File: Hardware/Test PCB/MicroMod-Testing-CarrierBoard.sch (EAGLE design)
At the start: 61 parts, among them J11 microSD, J12 SPI, J14 I2C, J2 JTAG, J3 QWIIC_RIGHT_ANGLE, J5 UART, J6 MICROMOD-2222-C, J8 Dedicated, U2 MCP73831, U5 AP7361C-33

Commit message: Finishes trace work on Test board - needs some silk
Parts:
- removed C8: 10uF, SparkFun-Capacitors:10UF-0603-6.3V-20%
- removed C9: 1.0uF, SparkFun-Capacitors:1.0UF-0603-16V-10%
- removed J14: I2C, SparkFun-Connectors:I2C_STANDARD_NO_SILK
- removed R1, R4: 2.2k, SparkFun-Resistors:2.2KOHM-0603-1/10W-1%
- added H6, H7: STAND-OFF, SparkFun-Hardware:STAND-OFF
- added J10: (no value), SparkFun-Connectors:CONN_08NO_SILK_FEMALE_PTH
- added J13: QWIIC_RIGHT_ANGLE, SparkFun-Connectors:QWIIC_CONNECTORJS-1MM
- J5: value UART -> (none); device SparkFun-Connectors:CONN_041X04_NO_SILK -> SparkFun-Connectors:CONN_08NO_SILK_FEMALE_PTH
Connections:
- net N$1 renamed OUT_MEAS
- removed net HEADER_!CS!: J12.5, J6.G0/BUS0
- removed net I2C_!INT!: J6.I2C_!INT!, J9.1
- removed net I2C_SCL: J14.4, J3.4, J6.I2C_SCL, R4.1
- removed net I2C_SDA: J14.3, J3.3, J6.I2C_SDA, R1.1
- new net !CS1: J12.5, J6.SPI_!CS!1
- new net A5: J10.7, J6.G9/ADC_D-/CAM_HSYNC
- new net A6: J10.8, J6.G10/ADC_D+/CAM_VSYNC
- new net CAN_RXI: J5.8, J6.CAN-RX
- new net CAN_TXO: J5.7, J6.CAN-TX
- new net D2: J10.6, J6.G0/BUS0
- new net D3: J10.5, J6.G1/BUS1
- new net D4: J10.4, J6.G2/BUS2
- new net D5: J10.3, J6.G3/BUS3
- new net D6: J10.2, J6.G4/BUS4
- new net D7: J10.1, J6.G5/BUS5
- new net D8/!INT: J6.G7/BUS7, J6.I2C_!INT!, J9.1
- new net I2S_CLK: J5.4, J6.AUD_BCLK
- new net I2S_SDI: J5.2, J6.AUD_IN/CAM_PCLK
- new net I2S_SDO: J5.1, J6.AUD_OUT/CAM_MCLK
- new net I2S_WS: J5.3, J6.AUD_LRCLK
- new net MISO1: J12.4, J6.SPI_MISO1
- new net MOSI1: J12.3, J6.SPI_MOSI1
- new net SCL: J3.4, J6.I2C_SCL
- new net SCL1: J13.4, J6.I2C_SCL1
- new net SCLK1: J12.2, J6.SPI_SCK1
- new net SDA: J3.3, J6.I2C_SDA
- new net SDA1: J13.3, J6.I2C_SDA1
- net 3.3V: now also J13.2; no longer C8.1, C9.1, J14.2, J5.4, JP1.2
- net GND: now also J13.1; no longer C8.2, C9.2, J14.1, J5.1
- net N$2: now also R10.1; no longer R4.2
- net N$3: now also R9.2; no longer R1.2
- net RX1: now also J5.6; no longer J5.2
- net SPI_MISO: no longer J12.4
- net SPI_MOSI: no longer J12.3
- net SPI_SCK: no longer J12.2
- net TX1: now also J5.5; no longer J5.3
- net VIN/3: now also JP1.2; no longer R10.1, R9.2
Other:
- note added: "Analog"
- note added: "Bus Connections - I2C, SPI, UART, I2S, CAN"
- note added: "Digital/Diff_Analog"
- note added: "I2C One"
- note added: "I2C Two"
- note added: "I2S/UART/CAN"
- note removed: "Qwiic"
- moved on the sheet: J12, J3, J8, J9, JP1, R10, R9

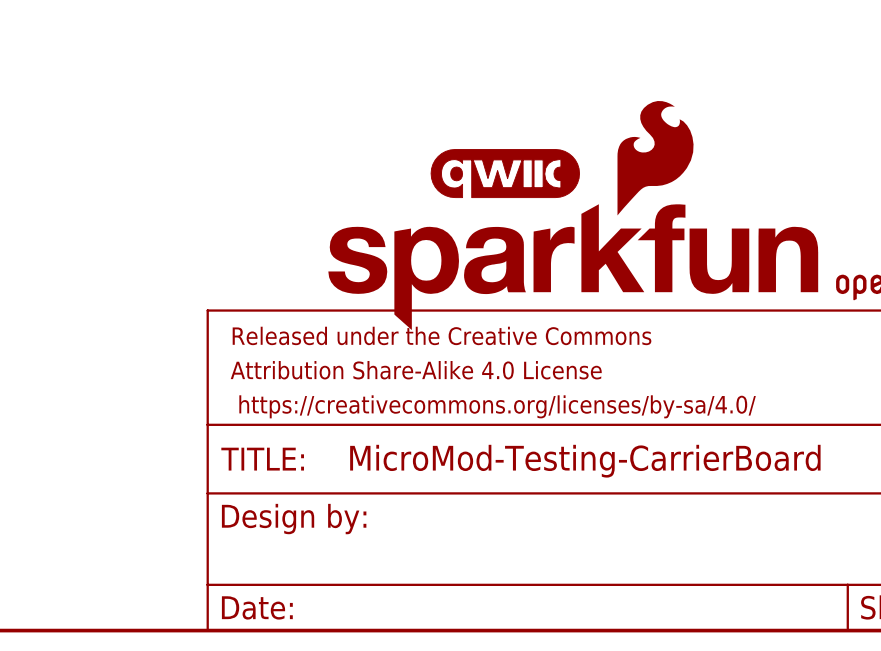
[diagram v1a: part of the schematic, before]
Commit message: Adds silk to Testbed and moves SWD header
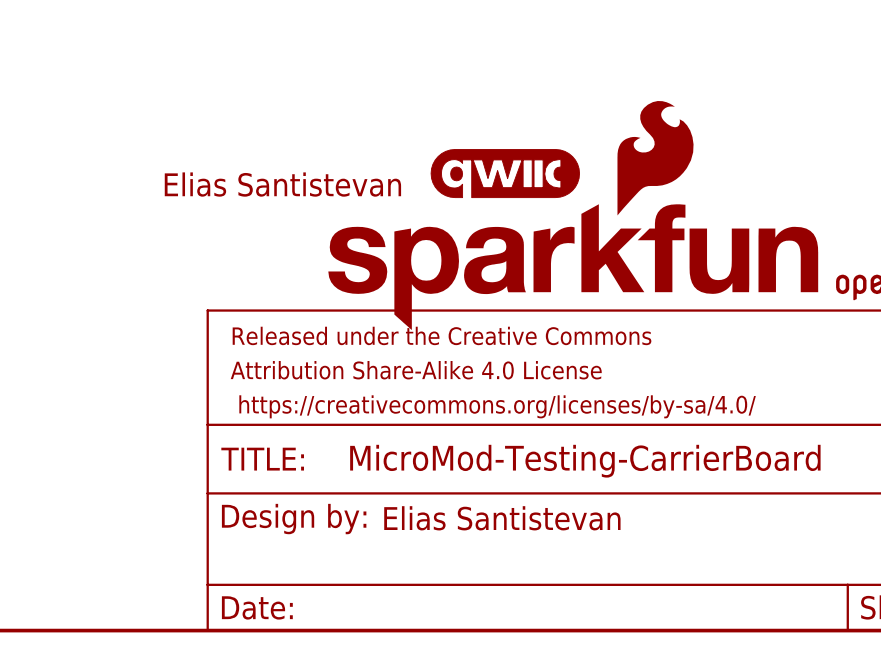
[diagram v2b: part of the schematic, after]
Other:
- note added: "Elias Santistevan"
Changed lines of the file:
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@@
 <wire x1="378.46" y1="160.02" x2="266.7" y2="160.02" width="0.1524" layer="97" style="longdash"/>
 <text x="274.32" y="152.4" size="2.54" layer="94" font="vector">Bus Connections - I2C, SPI, UART, I2S, CAN</text>
+<text x="349.504" y="11.176" size="2.54" layer="94">Elias Santistevan</text>
+<text x="325.12" y="48.26" size="2.54" layer="94">Elias Santistevan</text>
 </plain>
 <instances>

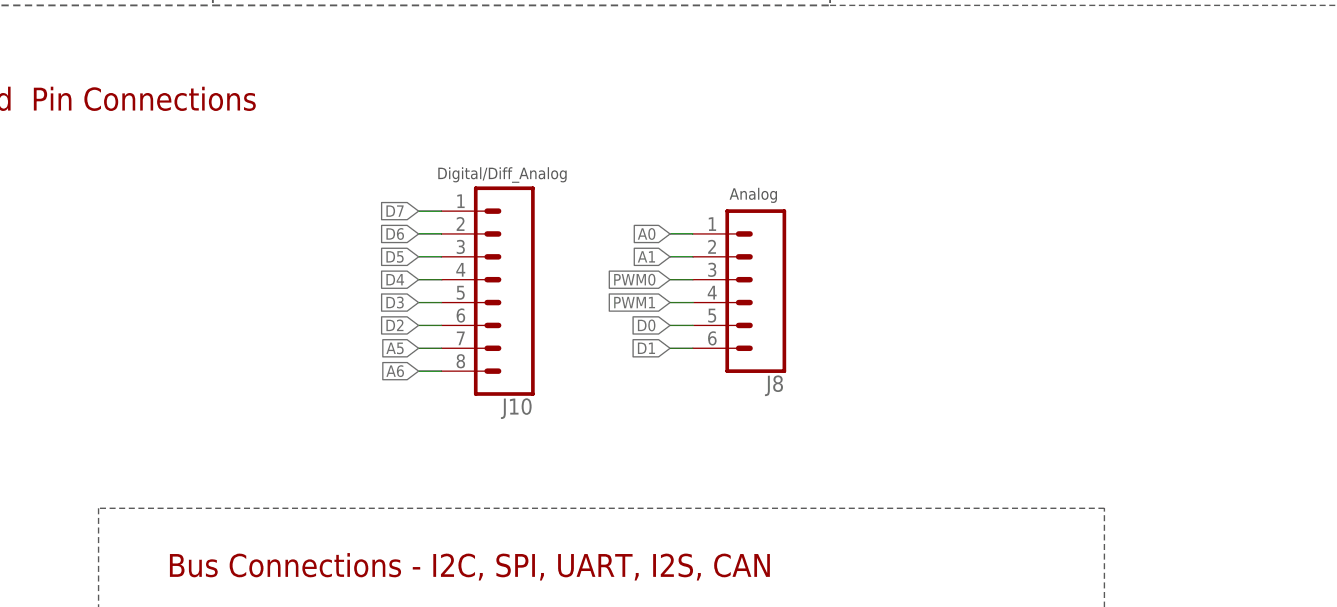
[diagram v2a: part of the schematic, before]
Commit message: Updates silk on testing carrier board
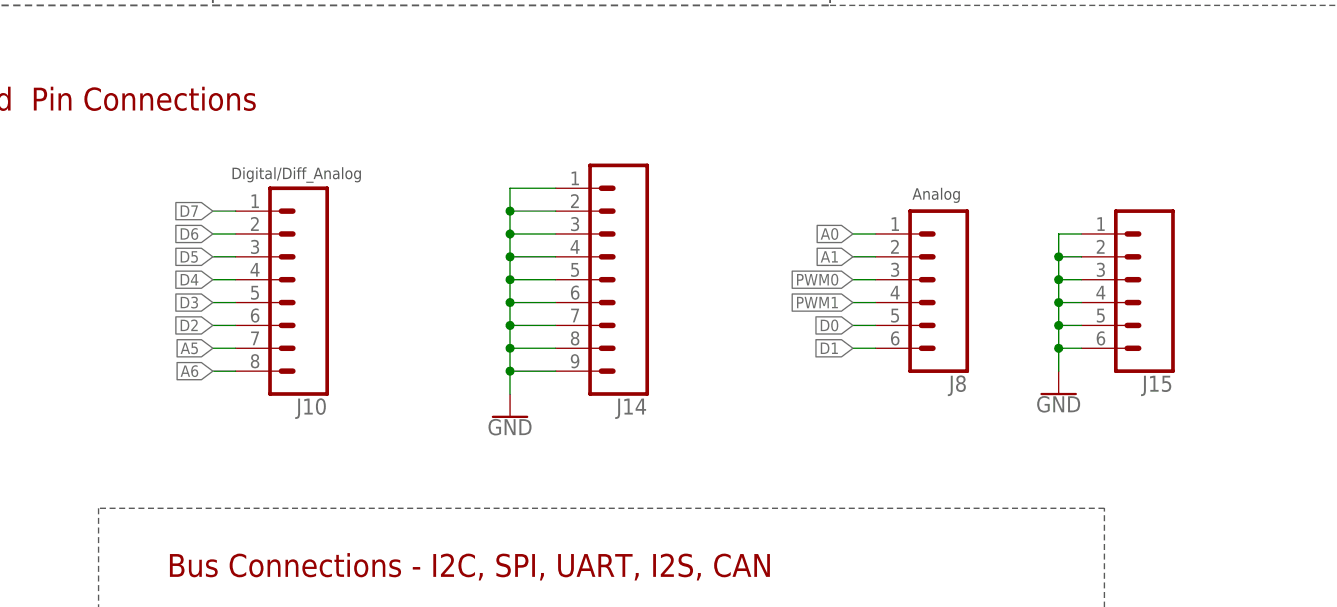
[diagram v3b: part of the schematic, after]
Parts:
- added J14: (no value), SparkFun-Connectors:CONN_09NO_SILK
- added J15: Dedicated, SparkFun-Connectors:CONN_06NO_SILK_NO_POP
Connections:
- net GND: now also J14.1, J14.2, J14.3, J14.4, J14.5, J14.6, J14.7, J14.8, J14.9, J15.1, J15.2, J15.3, J15.4, J15.5, J15.6
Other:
- moved on the sheet: J10, J8

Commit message: Updates testing carrier board with all nets added and half of teh new ones added
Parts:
- removed C3: 4.7uF, SparkFun-Capacitors:4.7UF-0603-35V-(20%)
- removed C4: 4.7uF, SparkFun-Capacitors:4.7UF-0603-6.3V-(10%)
- removed D2: Yellow, SparkFun-LED:LED-YELLOW0603
- removed D3: 3A/10V/280mV, SparkFun-DiscreteSemi:DIODE-SCHOTTKY-BAT60A
- removed H6, H7: STAND-OFF, SparkFun-Hardware:STAND-OFF
- removed J10: (no value), SparkFun-Connectors:CONN_08NO_SILK_FEMALE_PTH
- removed MEAS_BATT: JUMPER-COMBO_2_NC_TRACE, SparkFun-Jumpers:JUMPER-COMBO_2_NC_TRACE
- removed R6: 2.2k, SparkFun-Resistors:2.2KOHM-0603-1/10W-1%
- removed R7: 1k, SparkFun-Resistors:1KOHM-0603-1/10W-1%
- removed U2: MCP73831, SparkFun-IC-Power:MCP73831
- J14: device SparkFun-Connectors:CONN_09NO_SILK -> SparkFun-Connectors:CONN_12NO_SILK
- J4: value (none) -> USB_A_SMT_FEMALE; device SparkFun-Connectors:JST_2MM_MALE -> SparkFun-Connectors:USB_A_SMT_FEMALE
- J5: device SparkFun-Connectors:CONN_08NO_SILK_FEMALE_PTH -> SparkFun-Connectors:CONN_12NO_SILK
- J7: device SparkFun-Connectors:CONN_021X02_NO_SILK -> SparkFun-Connectors:CONN_12NO_SILK
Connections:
- net USB_D+ renamed USB_P
- net USB_D- renamed USB_N
- removed net 5V: C3.1, D2.A, D3.C, MEAS_BATT.1, U2.VIN
- removed net A5: J10.7, J6.G9/ADC_D-/CAM_HSYNC
- removed net A6: J10.8, J6.G10/ADC_D+/CAM_VSYNC
- removed net CHG_LED: R7.1, U2.STAT
- removed net D2: J10.6, J6.G0/BUS0
- removed net D3: J10.5, J6.G1/BUS1
- removed net D4: J10.4, J6.G2/BUS2
- removed net D5: J10.3, J6.G3/BUS3
- removed net D6: J10.2, J6.G4/BUS4
- removed net D7: J10.1, J6.G5/BUS5
- removed net D8/!INT: J6.G7/BUS7, J6.I2C_!INT!, J9.1
- removed net N$4: D2.C, R7.2
- removed net N$7: R6.2, U2.PROG
- removed net V_BATT: C4.1, D3.A, J4.+, J7.1, U2.VBAT
- new net CTS1: J5.5, J6.CTS1
- new net G0: J6.G0/BUS0, J7.10
- new net G1: J6.G1/BUS1, J7.9
- new net G10/ADC_P: J6.G10/ADC_D+/CAM_VSYNC, J7.12
- new net G11: J6.G11, J7.1
- new net G2: J6.G2/BUS2, J7.8
- new net G3: J6.G3/BUS3, J7.7
- new net G4: J6.G4/BUS4, J7.6
- new net G5: J6.G5/BUS5, J7.5
- new net G6: J6.G6/BUS6, J7.4
- new net G7: J6.G7/BUS7, J7.3
- new net G8: J6.G8, J7.2
- new net G9/ADC_N: J6.G9/ADC_D-/CAM_HSYNC, J7.11
- new net I2C_!INT: J6.I2C_!INT!, J9.1
- new net MCLK: J6.AUD_MCLK
- new net RTS1: J5.6, J6.RTS1
- new net RX2: J5.12, J6.RX2
- new net TX2: J5.11, J6.TX2
- new net USBHOST_N: J4.D-, J6.USBHOST_D-
- new net USBHOST_P: J4.D+, J6.USBHOST_D+
- net CAN_RXI: now also J5.10; no longer J5.8
- net CAN_TXO: now also J5.9; no longer J5.7
- net GND: now also J14.10, J14.11, J14.12, J4.GND, J4.SHLD; no longer C3.2, C4.2, J4.-, J7.2, R6.1, U2.VSS
- net RX1: now also J5.8; no longer J5.6
- net TX1: now also J5.7; no longer J5.5
- net VIN: no longer MEAS_BATT.2
- net V_USB: now also J4.VBUS
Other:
- note removed: "Charge current: 450mA (1000V/Rprog)"
- note removed: "LiPo Charger"
- note removed: "LiPo Range: 3.6-4.2V"
- note removed: "Open jumper to switch or measure power"
